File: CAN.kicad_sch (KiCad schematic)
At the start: 6 parts, among them U6 SIT1051TK/3

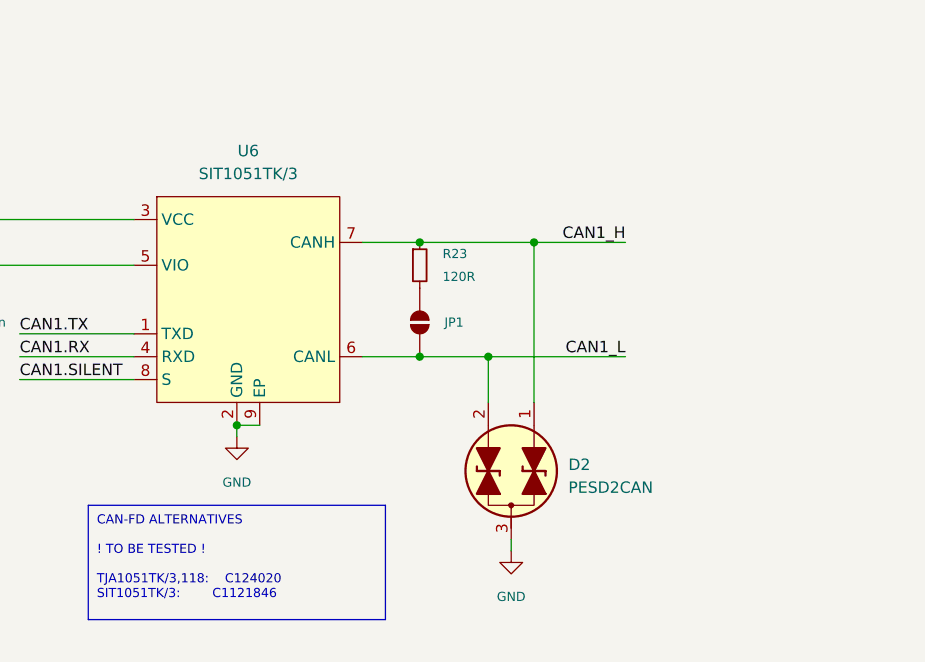
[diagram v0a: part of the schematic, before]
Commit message: fixed some BOM issues
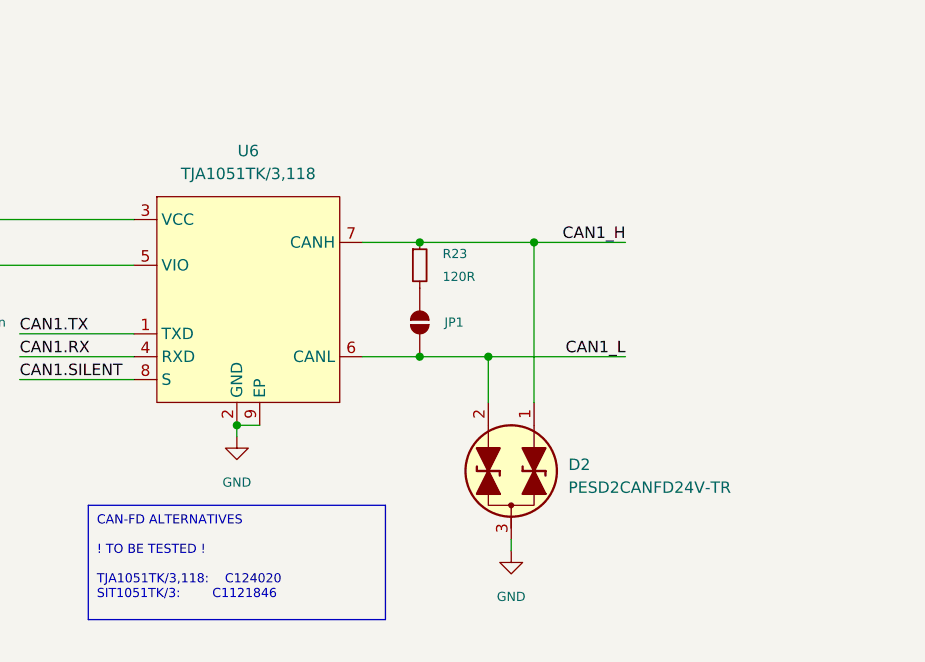
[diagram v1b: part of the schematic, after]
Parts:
- C26, C27: MPN GRM022R60J104KE15D -> CL05B104KO5NNNC
- D2: value PESD2CAN -> PESD2CANFD24V-TR
- U6: value SIT1051TK/3 -> TJA1051TK/3,118
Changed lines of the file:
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@@
 			)
 		)
-		(property "MPN" "GRM022R60J104KE15D"
+		(property "MPN" "CL05B104KO5NNNC"
 			(at 69.85 66.04 0)
 			(hide yes)
@@
 			)
 		)
-		(property "MPN" "GRM022R60J104KE15D"
+		(property "MPN" "CL05B104KO5NNNC"
 			(at 64.77 66.04 0)
 			(hide yes)
@@
 			)
 		)
-		(property "Value" "SIT1051TK/3"
+		(property "Value" "TJA1051TK/3,118"
 			(at 101.6 52.07 0)
 			(show_name no)
@@
 			)
 		)
-		(property "Value" "PESD2CAN"
+		(property "Value" "PESD2CANFD24V-TR"
 			(at 137.16 86.9314 90)
 			(show_name no)
